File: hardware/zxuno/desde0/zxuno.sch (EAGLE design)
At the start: 99 parts, among them J1 microUSB, J12 AUX_PW, J13 SWITCH, J3 RCA_FEMALE, J4 Audio, J5 EAR, J7 MINI-DIN6PTH, T1 BC846, U1 6SLX9TQG144, U2 FLASH-SPI-25XXSMD1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

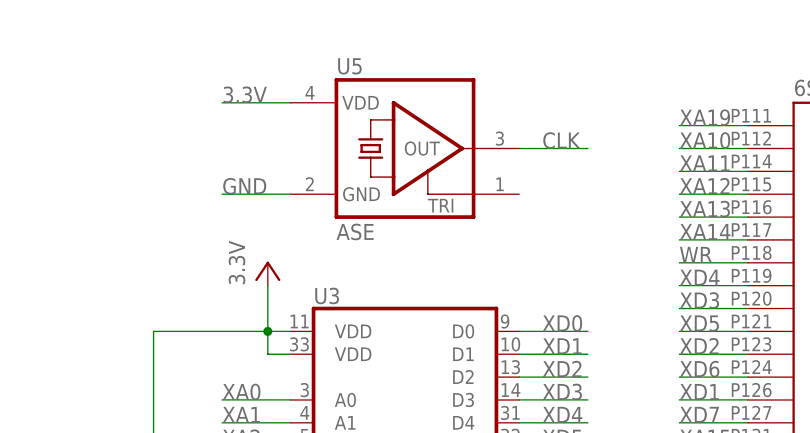
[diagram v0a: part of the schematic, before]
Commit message: 
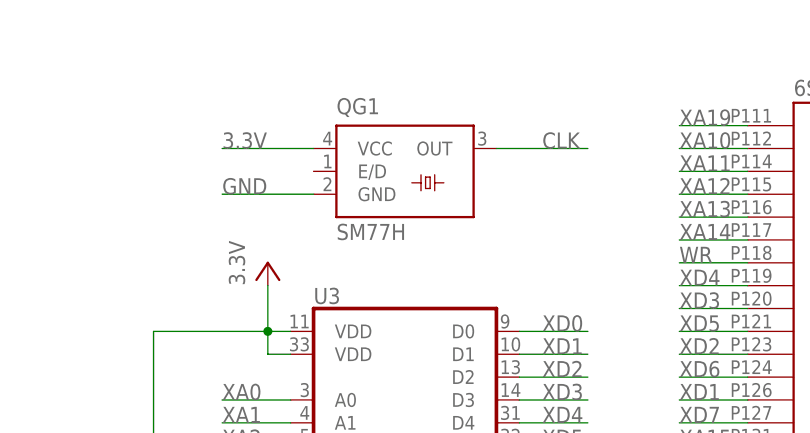
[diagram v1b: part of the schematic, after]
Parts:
- removed U5: ASE, crystal:ASE
- added QG1: SM77H, crystal:SM77H
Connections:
- net 3.3V: now also QG1.VCC; no longer U5.VDD
- net CLK: now also QG1.OUT; no longer U5.OUT
- net GND: now also QG1.GND; no longer U5.GND
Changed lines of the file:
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@@
 <part name="U1" library="xilinx_devices_V6" deviceset="6SLX9TQG144" device=""/>
 <part name="U3" library="GadgetFactory" deviceset="ISSI_SRAM_8BIT" device=""/>
-<part name="U5" library="crystal" deviceset="ASE" device=""/>
 <part name="3.3V" library="supply1" deviceset="VCC" device="" value="3.3V"/>
 <part name="GND1" library="supply1" deviceset="GND" device=""/>
@@
 <part name="C33" library="rcl" deviceset="C-EU" device="C0805" value="10uF"/>
 <part name="C34" library="rcl" deviceset="C-EU" device="C0805" value="10uF"/>
+<part name="QG1" library="crystal" deviceset="SM77H" device=""/>
 </parts>
 <sheets>
@@
 <instance part="U1" gate="BVCCINT" x="40.64" y="-109.22" rot="R180"/>
 <instance part="U3" gate="SRAM" x="-12.7" y="-5.08"/>
-<instance part="U5" gate="G$1" x="-2.54" y="83.82"/>
 <instance part="3.3V" gate="VCC" x="-17.78" y="71.12"/>
 <instance part="GND1" gate="1" x="-17.78" y="-7.62"/>
@@
 <instance part="C33" gate="G$1" x="251.46" y="-88.9" rot="R180"/>
 <instance part="C34" gate="G$1" x="261.62" y="-88.9" rot="R180"/>
+<instance part="QG1" gate="G$1" x="-2.54" y="81.28"/>
 </instances>
 <busses>
@@
 </segment>
 <segment>
-<pinref part="U5" gate="G$1" pin="VDD"/>
-<wire x1="-15.24" y1="88.9" x2="-22.86" y2="88.9" width="0.1524" layer="91"/>
-<label x="-22.86" y="88.9" size="1.778" layer="95"/>
+<wire x1="-12.7" y1="83.82" x2="-22.86" y2="83.82" width="0.1524" layer="91"/>
+<label x="-22.86" y="83.82" size="1.778" layer="95"/>
+<pinref part="QG1" gate="G$1" pin="VCC"/>
 </segment>
 <segment>
@@
 </segment>
 <segment>
-<pinref part="U5" gate="G$1" pin="GND"/>
-<wire x1="-15.24" y1="78.74" x2="-22.86" y2="78.74" width="0.1524" layer="91"/>
+<wire x1="-12.7" y1="78.74" x2="-22.86" y2="78.74" width="0.1524" layer="91"/>
 <label x="-22.86" y="78.74" size="1.778" layer="95"/>
+<pinref part="QG1" gate="G$1" pin="GND"/>
 </segment>
 <segment>
@@
 <net name="CLK" class="0">
 <segment>
-<pinref part="U5" gate="G$1" pin="OUT"/>
-<wire x1="10.16" y1="83.82" x2="17.78" y2="83.82" width="0.1524" layer="91"/>
+<wire x1="7.62" y1="83.82" x2="17.78" y2="83.82" width="0.1524" layer="91"/>
 <label x="12.7" y="83.82" size="1.778" layer="95"/>
-</segment>
-<segment>
+<pinref part="QG1" gate="G$1" pin="OUT"/>
+</segment>
+<segment>

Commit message: 
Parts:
- removed J3: RCA_FEMALE, Mio:RCA_FEMALE
- removed R25, R26: 2K, rcl:R-US_M0805
- added U$1: RCA_JACK_RCJ-04X_1, ZX_UNO_0_14:RCA_JACK_RCJ-04X_1
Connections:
- net JOY2 renamed JOY_RIGHT
- net JOY3 renamed JOY_LEFT
- net JOY4 renamed JOY_DOWN
- net JOY5 renamed JOY_FIRE2
- net JOY6 renamed JOY_UP
- net JOY7 renamed JOY_FIRE1
- net LEFT renamed AUDIO_LEFT
- net RIGHT renamed AUDIO_RIGHT
- removed net EXT1(WP): J9.2, R26.1, U1B2.IO_L12P_D1_MISO2_2, U2.WP
- removed net EXT2(HOLD): J10.2, R25.1, U1B2.IO_L12N_D2_MISO3_2, U2.HOLD
- removed net EXT3: J11.2, U1B2.IO_L14P_D11_2
- new net EXT6: J11.3, U1B2.IO_L14P_D11_2
- new net FLASH_HOLD: U1B2.IO_L12N_D2_MISO3_2, U2.HOLD
- new net FLASH_WP: U1B2.IO_L12P_D1_MISO2_2, U2.WP
- new net KEY: J10.3
- net 3.3V: no longer R25.2, R26.2
- net 5V: now also J9.3; no longer J9.1
- net GND: now also U$1.2; no longer J3.2
- net N$28: now also U$1.1; no longer J3.1
- net TCK: now also J9.1
- net TDI: now also J10.2
- net TDO: now also J9.2
- net TMS: now also J11.2

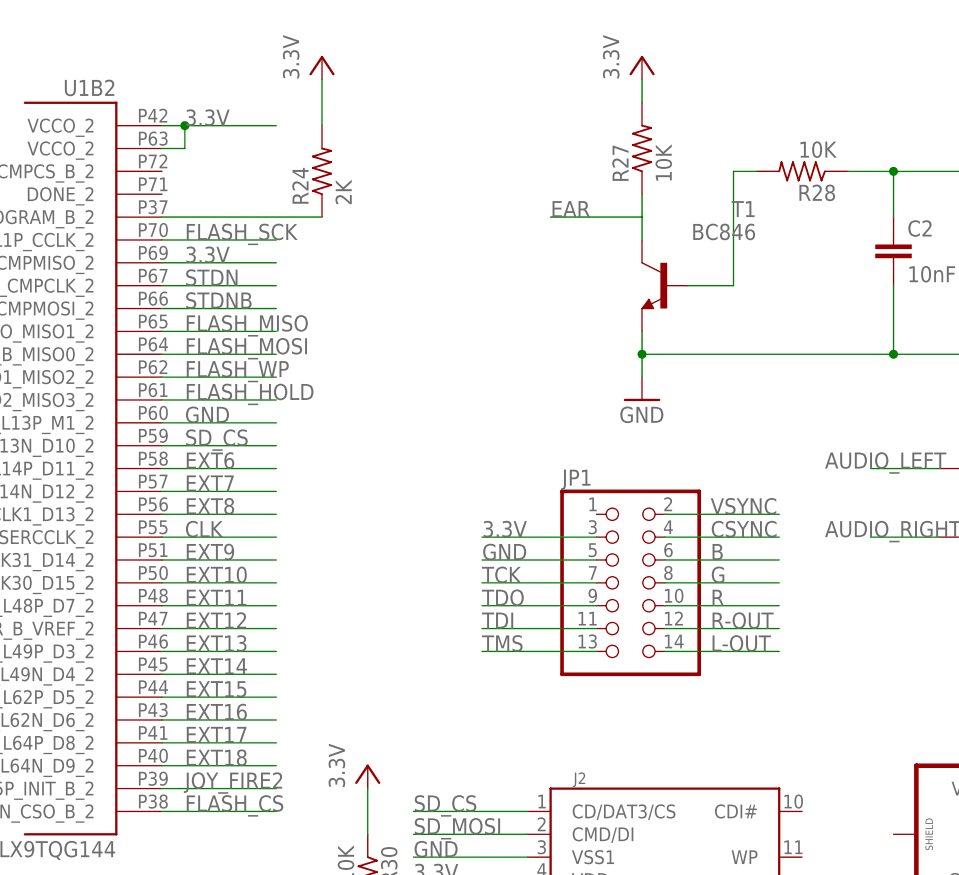
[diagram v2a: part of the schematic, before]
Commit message: 
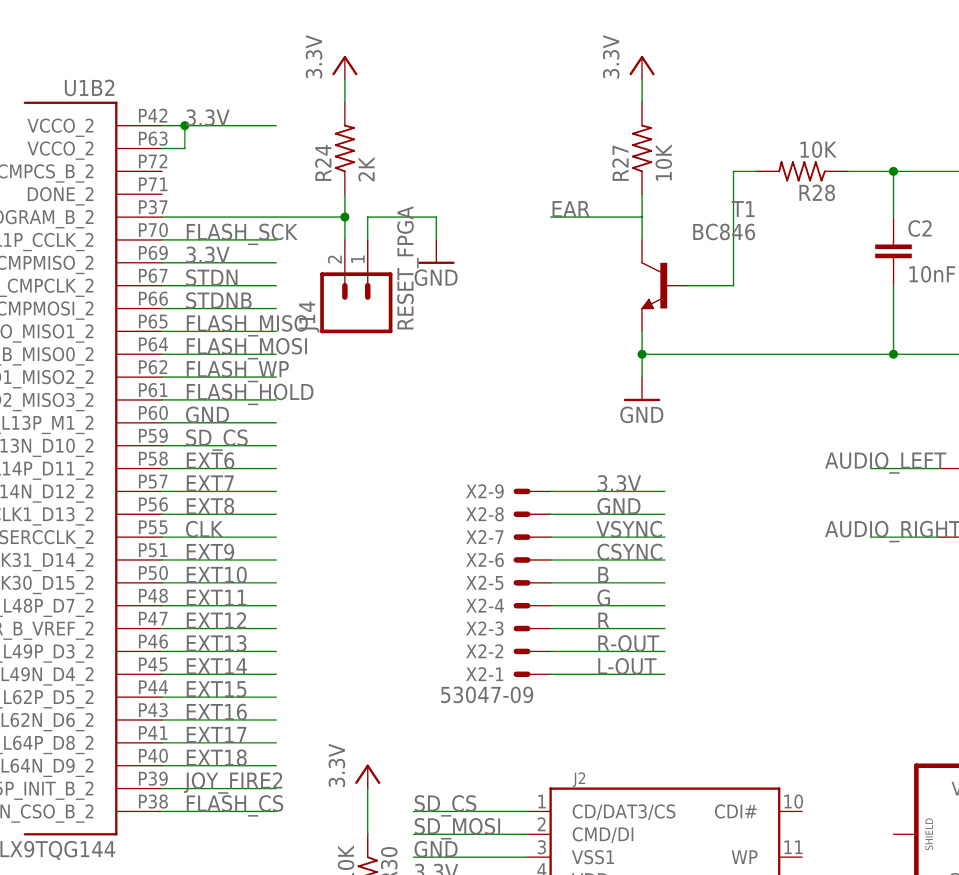
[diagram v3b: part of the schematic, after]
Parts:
- removed JP1: (no value), pinhead:PINHD-2X7
- added J14: RESET_FPGA, SparkFun-Connectors:M02POLAR
- added X2: 53047-09, con-molex:53047-09
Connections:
- net 3.3V: now also X2-9.S; no longer JP1.3
- net B: now also X2-5.S; no longer JP1.6
- net CSYNC: now also X2-6.S; no longer JP1.4
- net G: now also X2-4.S; no longer JP1.8
- net GND: now also J14.1, X2-8.S; no longer JP1.5
- net L-OUT: now also X2-1.S; no longer JP1.14
- net N$5: now also J14.2
- net R: now also X2-3.S; no longer JP1.10
- net R-OUT: now also X2-2.S; no longer JP1.12
- net TCK: no longer JP1.7
- net TDI: no longer JP1.11
- net TDO: no longer JP1.9
- net TMS: no longer JP1.13
- net VSYNC: now also X2-7.S; no longer JP1.2
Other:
- moved on the sheet: R24
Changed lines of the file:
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@@
 <part name="R15" library="rcl" deviceset="R-US_" device="M0805" value="510"/>
 <part name="R29" library="rcl" deviceset="R-US_" device="M0805" value="10K"/>
-<part name="JP1" library="pinhead" deviceset="PINHD-2X7" device=""/>
 <part name="R22" library="rcl" deviceset="R-US_" device="M0805" value="2K"/>
 <part name="R23" library="rcl" deviceset="R-US_" device="M0805" value="2K"/>
@@
 <part name="QG1" library="crystal" deviceset="SM77H" device=""/>
 <part name="U$1" library="ZX_UNO_0_14" deviceset="RCA_JACK_RCJ-04X_1" device=""/>
+<part name="J14" library="SparkFun-Connectors" deviceset="M02" device="POLAR" value="RESET_FPGA"/>
+<part name="GND18" library="supply1" deviceset="GND" device=""/>
+<part name="X2" library="con-molex" deviceset="53?-09" device="047"/>
 </parts>
 <sheets>
@@
 <instance part="5V" gate="VCC" x="-17.78" y="-40.64"/>
 <instance part="GND4" gate="1" x="-17.78" y="-68.58"/>
-<instance part="R24" gate="G$1" x="116.84" y="81.28" rot="R90"/>
-<instance part="3.3V2" gate="VCC" x="116.84" y="93.98"/>
+<instance part="R24" gate="G$1" x="119.38" y="83.82" rot="R90"/>
+<instance part="3.3V2" gate="VCC" x="119.38" y="93.98"/>
 <instance part="C9" gate="G$1" x="-22.86" y="-81.28" rot="R180"/>
 <instance part="C10" gate="G$1" x="-12.7" y="-81.28" rot="R180"/>
@@
 <instance part="R15" gate="G$1" x="213.36" y="81.28" rot="R180"/>
 <instance part="R29" gate="G$1" x="223.52" y="71.12" rot="R270"/>
-<instance part="JP1" gate="A" x="149.86" y="35.56"/>
 <instance part="R22" gate="G$1" x="190.5" y="48.26" rot="R180"/>
 <instance part="R23" gate="G$1" x="190.5" y="40.64" rot="R180"/>
@@
 <instance part="QG1" gate="G$1" x="-2.54" y="81.28"/>
 <instance part="U$1" gate="G$1" x="274.32" y="-104.14" rot="MR0"/>
+<instance part="J14" gate="G$1" x="121.92" y="66.04" rot="R90"/>
+<instance part="GND18" gate="1" x="129.54" y="71.12"/>
+<instance part="X2" gate="-1" x="139.7" y="25.4" rot="R180"/>
+<instance part="X2" gate="-2" x="139.7" y="27.94" rot="R180"/>
+<instance part="X2" gate="-3" x="139.7" y="30.48" rot="R180"/>
+<instance part="X2" gate="-4" x="139.7" y="33.02" rot="R180"/>
+<instance part="X2" gate="-5" x="139.7" y="35.56" rot="R180"/>
+<instance part="X2" gate="-6" x="139.7" y="38.1" rot="R180"/>
+<instance part="X2" gate="-7" x="139.7" y="40.64" rot="R180"/>
+<instance part="X2" gate="-8" x="139.7" y="43.18" rot="R180"/>
+<instance part="X2" gate="-9" x="139.7" y="45.72" rot="R180"/>
 </instances>
 <busses>
@@
 <pinref part="3.3V2" gate="VCC" pin="VCC"/>
 <pinref part="R24" gate="G$1" pin="2"/>
-<wire x1="116.84" y1="86.36" x2="116.84" y2="91.44" width="0.1524" layer="91"/>
+<wire x1="119.38" y1="88.9" x2="119.38" y2="91.44" width="0.1524" layer="91"/>
 </segment>
 <segment>
@@
 </segment>
 <segment>
-<wire x1="147.32" y1="40.64" x2="134.62" y2="40.64" width="0.1524" layer="91"/>
-<label x="134.62" y="40.64" size="1.778" layer="95"/>
-<pinref part="JP1" gate="A" pin="3"/>
+<wire x1="154.94" y1="45.72" x2="142.24" y2="45.72" width="0.1524" layer="91"/>
+<label x="147.32" y="45.72" size="1.778" layer="95"/>
+<pinref part="X2" gate="-9" pin="S"/>
 </segment>
 <segment>
@@
 </segment>
 <segment>
-<wire x1="147.32" y1="38.1" x2="134.62" y2="38.1" width="0.1524" layer="91"/>
-<label x="134.62" y="38.1" size="1.778" layer="95"/>
-<pinref part="JP1" gate="A" pin="5"/>
+<wire x1="154.94" y1="43.18" x2="142.24" y2="43.18" width="0.1524" layer="91"/>
+<label x="147.32" y="43.18" size="1.778" layer="95"/>
+<pinref part="X2" gate="-8" pin="S"/>
 </segment>
 <segment>
@@
 <wire x1="152.4" y1="-86.36" x2="152.4" y2="-83.82" width="0.1524" layer="91"/>
 </segment>
+<segment>
+<pinref part="J14" gate="G$1" pin="1"/>
+<wire x1="121.92" y1="73.66" x2="121.92" y2="76.2" width="0.1524" layer="91"/>
+<pinref part="GND18" gate="1" pin="GND"/>
+<wire x1="121.92" y1="76.2" x2="129.54" y2="76.2" width="0.1524" layer="91"/>
+<wire x1="129.54" y1="76.2" x2="129.54" y2="73.66" width="0.1524" layer="91"/>
+</segment>
 </net>
 <net name="XA0" class="0">
@@
 </segment>
 <segment>
-<wire x1="167.64" y1="43.18" x2="154.94" y2="43.18" width="0.1524" layer="91"/>
-<label x="160.02" y="43.18" size="1.778" layer="95"/>
-<pinref part="JP1" gate="A" pin="2"/>
+<wire x1="154.94" y1="40.64" x2="142.24" y2="40.64" width="0.1524" layer="91"/>
+<label x="147.32" y="40.64" size="1.778" layer="95"/>
+<pinref part="X2" gate="-7" pin="S"/>
 </segment>
 </net>
@@
 </segment>
 <segment>
-<wire x1="167.64" y1="40.64" x2="154.94" y2="40.64" width="0.1524" layer="91"/>
-<label x="160.02" y="40.64" size="1.778" layer="95"/>
-<pinref part="JP1" gate="A" pin="4"/>
+<wire x1="154.94" y1="38.1" x2="142.24" y2="38.1" width="0.1524" layer="91"/>
+<label x="147.32" y="38.1" size="1.778" layer="95"/>
+<pinref part="X2" gate="-6" pin="S"/>
 </segment>
 <segment>
@@
 <pinref part="R8" gate="G$1" pin="1"/>
 <wire x1="-12.7" y1="-60.96" x2="-20.32" y2="-60.96" width="0.1524" layer="91"/>
-</segment>
-</net>
-<net name="N$5" class="0">
-<segment>
-<pinref part="U1" gate="B2" pin="PROGRAM_B_2"/>
-<pinref part="R24" gate="G$1" pin="1"/>
-<wire x1="99.06" y1="76.2" x2="116.84" y2="76.2" width="0.1524" layer="91"/>
 </segment>
 </net>
@@
 <net name="TMS" class="0">
 <segment>
-<wire x1="147.32" y1="27.94" x2="134.62" y2="27.94" width="0.1524" layer="91"/>
-<label x="134.62" y="27.94" size="1.778" layer="95"/>
-<pinref part="JP1" gate="A" pin="13"/>
-</segment>
-<segment>
 <wire x1="35.56" y1="-137.16" x2="25.4" y2="-137.16" width="0.1524" layer="91"/>
 <label x="30.48" y="-137.16" size="1.778" layer="95" rot="MR0"/>
@@
 <net name="B" class="0">
 <segment>
-<wire x1="167.64" y1="38.1" x2="154.94" y2="38.1" width="0.1524" layer="91"/>
-<label x="160.02" y="38.1" size="1.778" layer="95"/>
-<pinref part="JP1" gate="A" pin="6"/>
+<wire x1="154.94" y1="35.56" x2="142.24" y2="35.56" width="0.1524" layer="91"/>
+<label x="147.32" y="35.56" size="1.778" layer="95"/>
+<pinref part="X2" gate="-5" pin="S"/>
 </segment>
 <segment>
@@
 <net name="G" class="0">
 <segment>
-<wire x1="167.64" y1="35.56" x2="154.94" y2="35.56" width="0.1524" layer="91"/>
-<label x="160.02" y="35.56" size="1.778" layer="95"/>
-<pinref part="JP1" gate="A" pin="8"/>
+<wire x1="154.94" y1="33.02" x2="142.24" y2="33.02" width="0.1524" layer="91"/>
+<label x="147.32" y="33.02" size="1.778" layer="95"/>
+<pinref part="X2" gate="-4" pin="S"/>
 </segment>
 <segment>
@@
 <net name="R" class="0">
 <segment>
-<wire x1="167.64" y1="33.02" x2="154.94" y2="33.02" width="0.1524" layer="91"/>
-<label x="160.02" y="33.02" size="1.778" layer="95"/>
-<pinref part="JP1" gate="A" pin="10"/>
+<wire x1="154.94" y1="30.48" x2="142.24" y2="30.48" width="0.1524" layer="91"/>
+<label x="147.32" y="30.48" size="1.778" layer="95"/>
+<pinref part="X2" gate="-3" pin="S"/>
 </segment>
 <segment>
@@
 <net name="R-OUT" class="0">
 <segment>
-<wire x1="167.64" y1="30.48" x2="154.94" y2="30.48" width="0.1524" layer="91"/>
-<label x="160.02" y="30.48" size="1.778" layer="95"/>
-<pinref part="JP1" gate="A" pin="12"/>
+<wire x1="154.94" y1="27.94" x2="142.24" y2="27.94" width="0.1524" layer="91"/>
+<label x="147.32" y="27.94" size="1.778" layer="95"/>
+<pinref part="X2" gate="-2" pin="S"/>
 </segment>
 <segment>
@@
 <net name="L-OUT" class="0">
 <segment>
-<wire x1="167.64" y1="27.94" x2="154.94" y2="27.94" width="0.1524" layer="91"/>
-<label x="160.02" y="27.94" size="1.778" layer="95"/>
-<pinref part="JP1" gate="A" pin="14"/>
+<wire x1="154.94" y1="25.4" x2="142.24" y2="25.4" width="0.1524" layer="91"/>
+<label x="147.32" y="25.4" size="1.778" layer="95"/>
+<pinref part="X2" gate="-1" pin="S"/>
 </segment>
 <segment>
@@
 <net name="TCK" class="0">
 <segment>
-<wire x1="147.32" y1="35.56" x2="134.62" y2="35.56" width="0.1524" layer="91"/>
-<label x="134.62" y="35.56" size="1.778" layer="95"/>
-<pinref part="JP1" gate="A" pin="7"/>
-</segment>
-<segment>
 <wire x1="35.56" y1="-129.54" x2="25.4" y2="-129.54" width="0.1524" layer="91"/>
 <label x="30.48" y="-129.54" size="1.778" layer="95" rot="MR0"/>
@@
 <net name="TDO" class="0">
 <segment>
-<wire x1="147.32" y1="33.02" x2="134.62" y2="33.02" width="0.1524" layer="91"/>
-<label x="134.62" y="33.02" size="1.778" layer="95"/>
-<pinref part="JP1" gate="A" pin="9"/>
-</segment>
-<segment>
 <wire x1="35.56" y1="-134.62" x2="25.4" y2="-134.62" width="0.1524" layer="91"/>
 <label x="30.48" y="-134.62" size="1.778" layer="95" rot="MR0"/>
@@
 </net>
 <net name="TDI" class="0">
-<segment>
-<wire x1="147.32" y1="30.48" x2="134.62" y2="30.48" width="0.1524" layer="91"/>
-<label x="134.62" y="30.48" size="1.778" layer="95"/>
-<pinref part="JP1" gate="A" pin="11"/>
-</segment>
 <segment>
 <wire x1="35.56" y1="-132.08" x2="25.4" y2="-132.08" width="0.1524" layer="91"/>
@@
 </segment>
 </net>
+<net name="N$5" class="0">
+<segment>
+<pinref part="U1" gate="B2" pin="PROGRAM_B_2"/>
+<wire x1="99.06" y1="76.2" x2="119.38" y2="76.2" width="0.1524" layer="91"/>
+<pinref part="R24" gate="G$1" pin="1"/>
+<pinref part="J14" gate="G$1" pin="2"/>
+<wire x1="119.38" y1="78.74" x2="119.38" y2="76.2" width="0.1524" layer="91"/>
+<junction x="119.38" y="76.2"/>
+<wire x1="119.38" y1="76.2" x2="119.38" y2="73.66" width="0.1524" layer="91"/>
+</segment>
+</net>

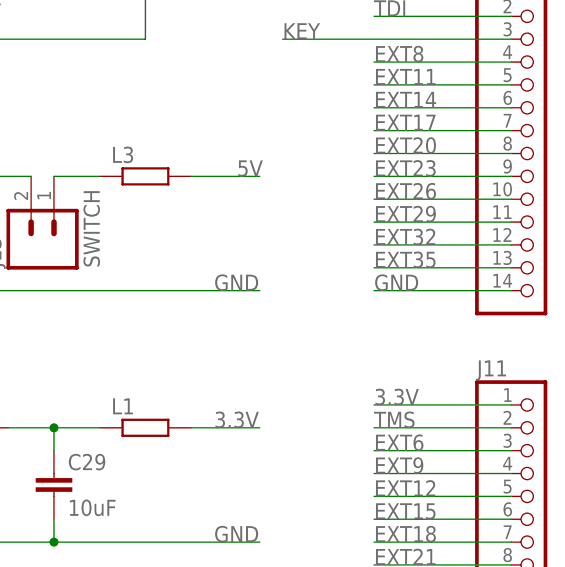
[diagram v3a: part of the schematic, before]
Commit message: 
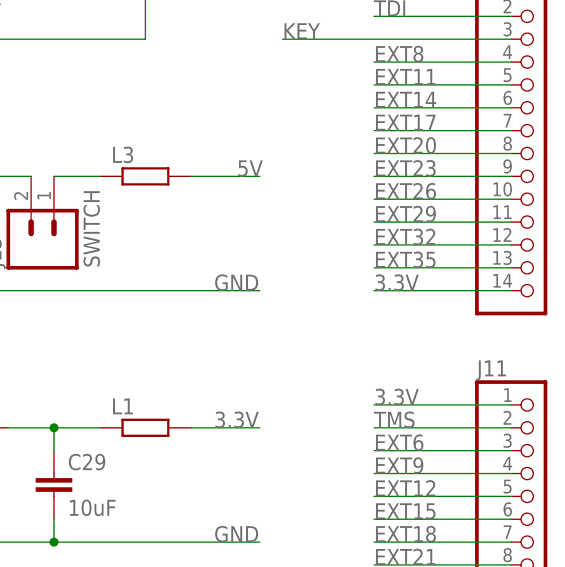
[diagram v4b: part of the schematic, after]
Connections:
- net 3.3V: now also J10.14
- net GND: no longer J10.14
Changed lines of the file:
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@@
 <pinref part="J11" gate="A" pin="1"/>
+</segment>
+<segment>
+<wire x1="261.62" y1="0" x2="276.86" y2="0" width="0.1524" layer="91"/>
+<label x="261.62" y="0" size="1.778" layer="95"/>
+<pinref part="J10" gate="A" pin="14"/>
 </segment>
 </net>
@@
 </segment>
 <segment>
-<wire x1="261.62" y1="0" x2="276.86" y2="0" width="0.1524" layer="91"/>
-<label x="261.62" y="0" size="1.778" layer="95"/>
-<pinref part="J10" gate="A" pin="14"/>
-</segment>
-<segment>
